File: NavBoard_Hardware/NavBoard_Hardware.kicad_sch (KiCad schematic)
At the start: 1 part, among them U5 Teensy4.1

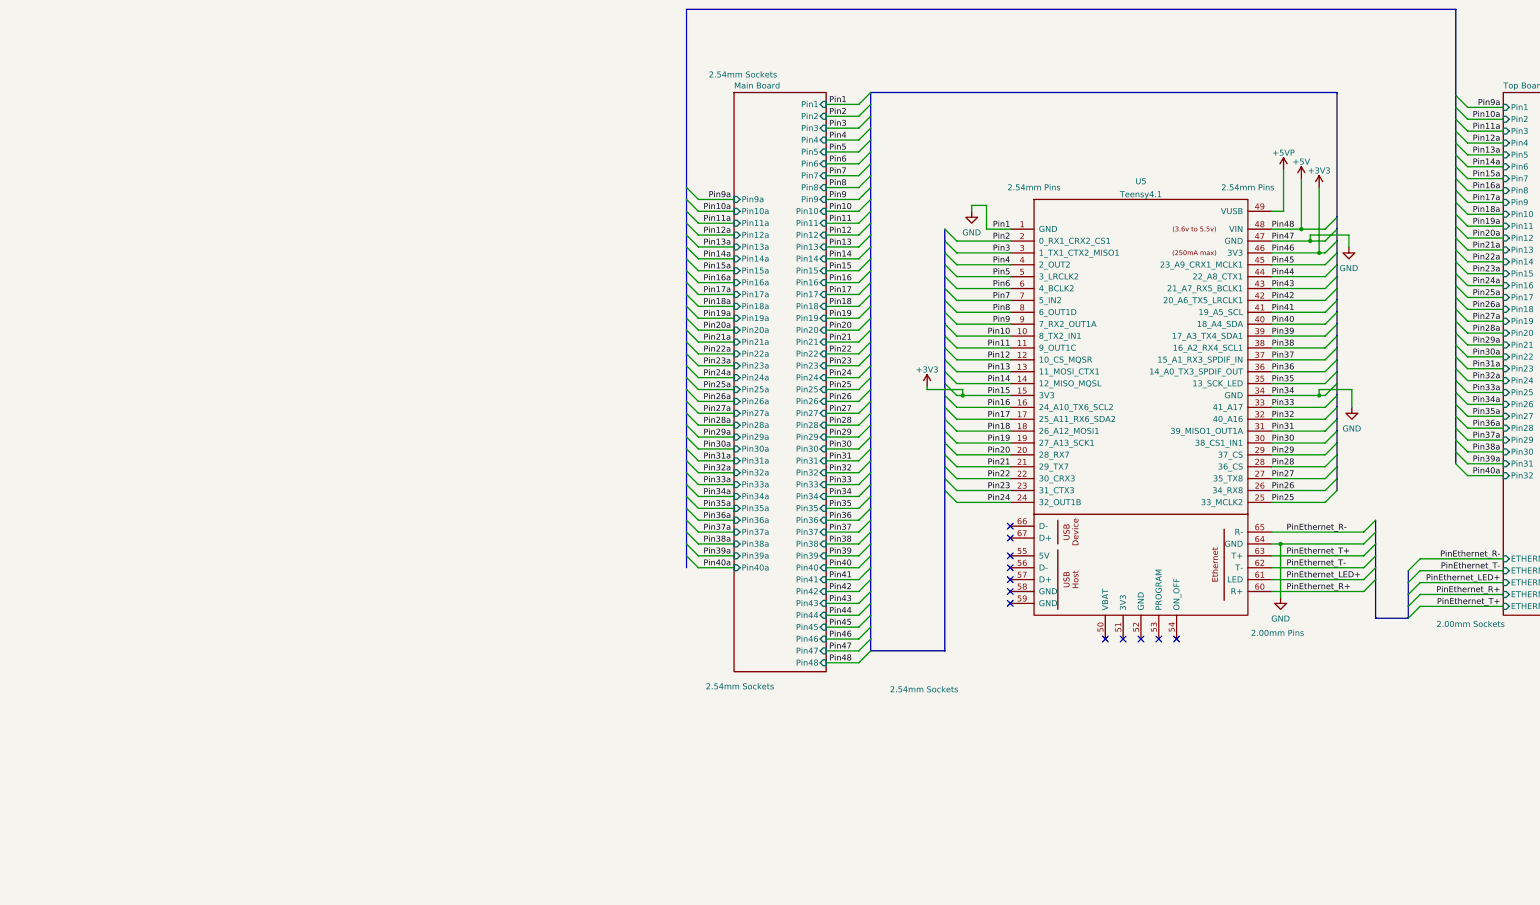
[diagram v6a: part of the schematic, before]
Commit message: Realized this could all fit on a single board
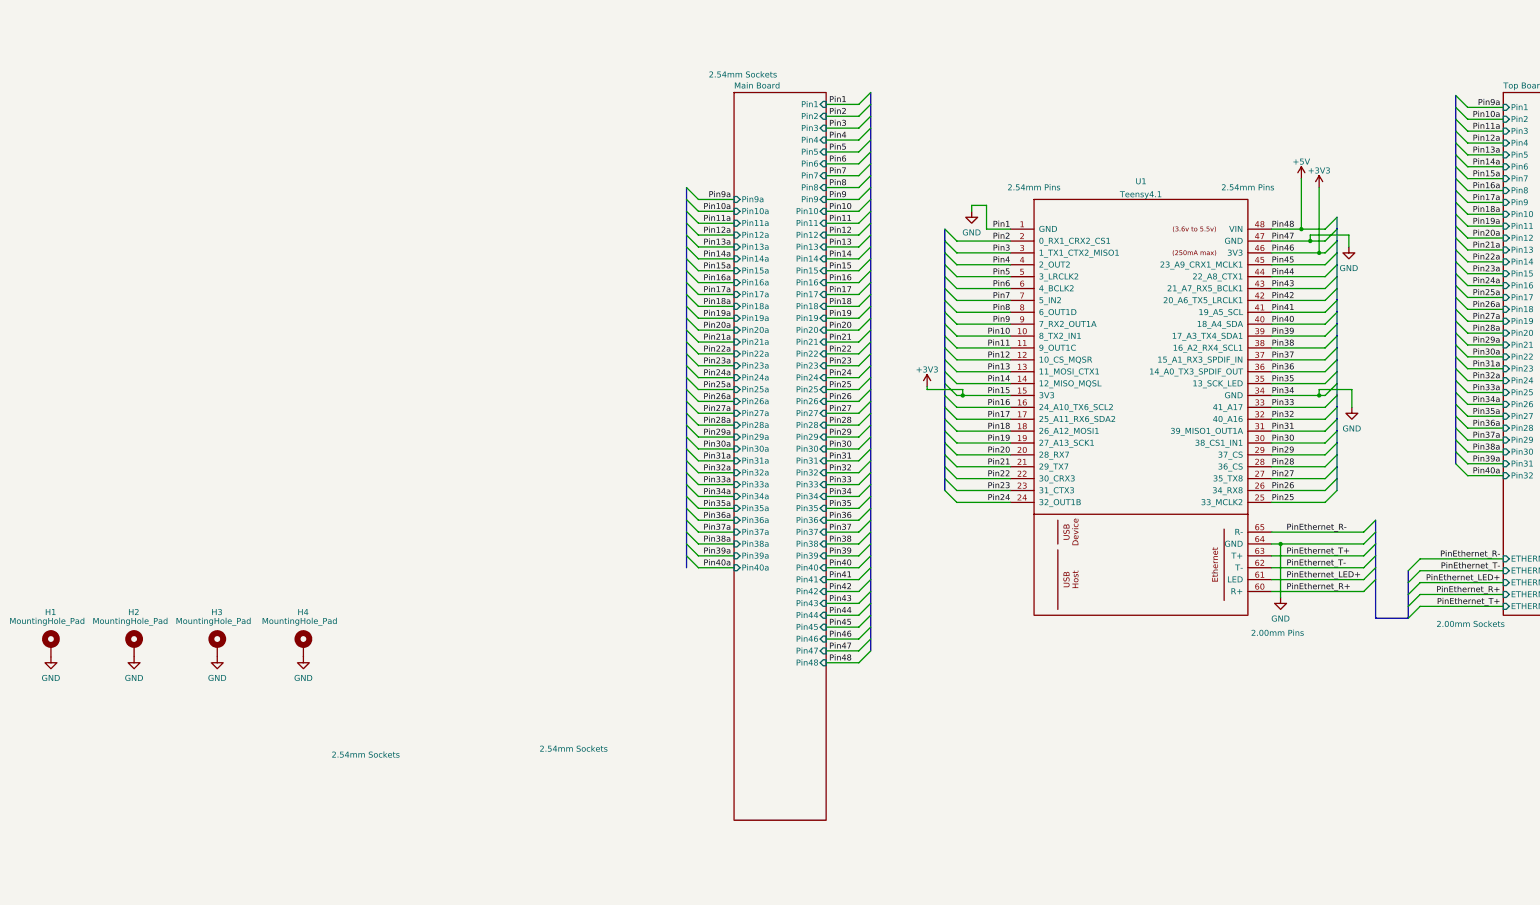
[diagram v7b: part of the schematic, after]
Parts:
- added H1, H2, H3, H4: MountingHole_Pad, symbol Mechanical:MountingHole_Pad
- U1: renamed from U5; footprint Nav_Board:Teensy41_Suspended -> Nav_Board:Teensy41
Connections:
- net GND: now also H1.1, H2.1, H3.1, H4.1
- removed net +5VP: U1.49 (VUSB)
- no-connect marks 12 -> 0

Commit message: Most connections made on schematic
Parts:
- added C1: 0.1uF, Capacitor_SMD:C_0603_1608Metric_Pad1.08x0.95mm_HandSolder, symbol Device:C_Polarized_US
- added Conn1: AndersonPP, MRDT_Connectors:Anderson_2_Vertical_Sidy_by_Side, symbol MRDT_Connectors:AndersonPP
- added D1: BLUE, LED_SMD:LED_0603_1608Metric_Pad1.05x0.95mm_HandSolder, symbol Device:LED
- added D2, D3, D4: GREEN, LED_SMD:LED_0603_1608Metric_Pad1.05x0.95mm_HandSolder, symbol Device:LED
- added D5: RED, LED_SMD:LED_0603_1608Metric_Pad1.05x0.95mm_HandSolder, symbol Device:LED
- added J1: 6 Pin Molex Micro-Fit, Connector_Molex:Molex_Micro-Fit_3.0_43650-0600_1x06_P3.00mm_Horizontal, symbol Connector_Generic:Conn_01x06
- added J2: Ethernet Jack w/ Magnetics, Connector_RJ:RJ45_Cetus_J1B1211CCD_Horizontal, symbol Connector:8P8C_LED_Shielded
- added R1, R2: 0ohm, Resistor_SMD:R_0603_1608Metric_Pad0.98x0.95mm_HandSolder, symbol Device:R_US
- added R15, R16, R17, R18, R5: 100Ω, Resistor_SMD:R_0603_1608Metric_Pad0.98x0.95mm_HandSolder, symbol Device:R_US
- added R3, R4, R6, R7: 4.7k, Resistor_SMD:R_0603_1608Metric_Pad0.98x0.95mm_HandSolder, symbol Device:R_US
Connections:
- net +3V3: now also R15.1, R16.1, R17.1, R18.1
- net +5V: now also J1.1 (Pin_1), R5.1
- net ETHERNET_LED: now also J2.10
- net ETHERNET_RX+: now also J2.4
- net ETHERNET_RX-: now also J2.6
- net ETHERNET_TX+: now also J2.1
- net ETHERNET_TX-: now also J2.3
- net GND: now also C1.2, Conn1.1 (GND), D1.1 (K), D5.1 (K), J1.2 (Pin_2), J2.13, J2.8, J2.9, R3.2, R4.2, R6.2, R7.2
- net Pin10 renamed BHI-SDA
- net BHI-SDA: now also R7.1
- net Pin11 renamed BHI-SCL
- net BHI-SCL: now also R6.1
- net Pin12: no longer names the net of U1.12 (10_CS_MQSR)
- net Pin13: no longer names the net of U1.13 (11_MOSI_CTX1)
- net Pin14 renamed ICM-SCLK
- net Pin16: no longer names the net of U1.16 (24_A10_TX6_SCL2)
- net Pin17: no longer names the net of U1.17 (25_A11_RX6_SDA2)
- net Pin18: no longer names the net of U1.18 (26_A12_MOSI1)
- net Pin19: no longer names the net of U1.19 (27_A13_SCK1)
- net Pin2: no longer names the net of U1.2 (0_RX1_CRX2_CS1)
- net Pin20: no longer names the net of U1.20 (28_RX7)
- net Pin21: no longer names the net of U1.21 (29_TX7)
- net Pin22 renamed GPS-TX
- net GPS-TX: now also J1.3 (Pin_3)
- net Pin23 renamed GPS-RX
- net GPS-RX: now also J1.4 (Pin_4)
- net Pin24: no longer names the net of U1.24 (32_OUT1B)
- net Pin25: no longer names the net of U1.25 (33_MCLK2)
- net Pin26: no longer names the net of U1.26 (34_RX8)
- net Pin27: no longer names the net of U1.27 (35_TX8)
- net Pin28: no longer names the net of U1.28 (36_CS)
- net Pin29: no longer names the net of U1.29 (37_CS)
- net Pin3: no longer names the net of U1.3 (1_TX1_CTX2_MISO1)
- net Pin30: no longer names the net of U1.30 (38_CS1_IN1)
- net Pin31: no longer names the net of U1.31 (39_MISO1_OUT1A)
- net Pin32 renamed GPS-SDA
- net GPS-SDA: now also J1.5 (Pin_5), R2.1
- net Pin33 renamed GPS-SCL
- net GPS-SCL: now also J1.6 (Pin_6), R1.1
- net Pin35 renamed ICM-MISO
- net Pin36 renamed ICM-MOSI
- net Pin37 renamed ICM-CS
- net Pin38: no longer names the net of U1.38 (16_A2_RX4_SCL1)
- net Pin39: no longer names the net of U1.39 (17_A3_TX4_SDA1)
- net Pin4: no longer names the net of U1.4 (2_OUT2)
- net Pin40: no longer names the net of U1.40 (18_A4_SDA)
- net Pin41: no longer names the net of U1.41 (19_A5_SCL)
- net Pin42: no longer names the net of U1.42 (20_A6_TX5_LRCLK1)
- net Pin43: no longer names the net of U1.43 (21_A7_RX5_BCLK1)
- net Pin44: no longer names the net of U1.44 (22_A8_CTX1)
- net Pin45: no longer names the net of U1.45 (23_A9_CRX1_MCLK1)
- net Pin5: no longer names the net of U1.5 (3_LRCLK2)
- net Pin6: no longer names the net of U1.6 (4_BCLK2)
- net Pin7: no longer names the net of U1.7 (5_IN2)
- net Pin8: no longer names the net of U1.8 (6_OUT1D)
- net Pin9: no longer names the net of U1.9 (7_RX2_OUT1A)
- new net: R2.2, R3.1
- new net: D4.2 (A), R17.2
- new net: D5.2 (A), R18.2
- new net: D1.2 (A), R5.2
- new net: D2.2 (A), R15.2
- new net: R1.2, R4.1
- new net: D3.2 (A), R16.2
- new net: C1.1, J2.2, J2.5
- new net +12V: Conn1.2 (V+Log)
- new net I2C_LED: D2.1 (K)
- new net SPI_LED: D4.1 (K)
- new net UART_LED: D3.1 (K)
- no-connect marks 0 -> 3
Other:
- removed sheet Main Board
- removed sheet Top Board
- added sheet IMU #1 - BHI160B (component_sheets\BHI160B.kicad_sch)
- added sheet IMU #2 - ICM-20608 (component_sheets\ICM-20608.kicad_sch)
- added sheet OKI - 5V (component_sheets\OKI-5V.kicad_sch)
- note added: "3V3) Red LEDs: 18mA @ 2Vf, 68-100Ω 3V3) Green LEDs: 18mA @ 2.2Vf, 68-100Ω 5v) Blue LEDs: 20mA @ 3.4Vf, 80-100Ω"
- note added: "Ethernet Jack"
- note added: "GPS"
- note added: "I2C Address Selection: HIGH = 0x29 LOW = 0x28"
- note added: "IMU #1 BHI160B"
- note added: "IMU #2 ICM-20608"
- note added: "Link/Activity Indicator LED: - Blinking = There is activity on this port. - Off = No link is established."
- note added: "Power"
- note added: "Speed Indicator LED: - Amber on = Operating as a Gigabit connection (1000 Mbps). - Green on = Operating as a 100-Mbps connection. - Off = Operating as a 10-Mbps connection."
- note added: "Status LEDs"
- moved on the sheet: H1, H2, H3, H4, U1
